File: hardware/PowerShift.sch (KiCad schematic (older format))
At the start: 47 parts

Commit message: RS232 expansion
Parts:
- removed D?: LED_ALT, symbol LED_ALT
- removed J?: I2C, symbol Conn_01x04
- removed R?: 1k, symbol R
- added C1: 100u, symbol C
- added J6: SHIFT_IN, symbol Conn_01x08
- C2, C4: renamed from C?; value C -> 10u
- C3: renamed from C?; value C -> 100u
- J2: renamed from J?; value USB_A -> MICRO_USB
- gave numbers to parts that had none: 40
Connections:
- net labels added: RX, TX, XCK
- wire segments 273 -> 279
- no-connect marks 21 -> 19
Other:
- moved on the sheet: C15, C16, C2, C3, C4, D1, J1, J10, J2, J5, J7, JMP1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

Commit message: JST 5 pin common part
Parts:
- removed J13: Conn_01x04, symbol Conn_01x04
- added J14: JST-ZR, symbol Conn_01x05
- R3: value R -> Rntc
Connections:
- wire segments 279 -> 281
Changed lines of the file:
@@
 P 5300 4750
 F 0 "R3" H 5350 4800 50  0000 L CNN
-F 1 "R" H 5350 4700 50  0000 L CNN
+F 1 "Rntc" H 5350 4700 50  0000 L CNN
 F 2 "" V 5230 4750 50  0001 C CNN
 F 3 "" H 5300 4750 50  0001 C CNN
@@
 	1    0    0    -1
 $EndComp
-$Comp
-L Conn_01x04 J13
-U 1 1 5B31B710
-P 5600 5350
-F 0 "J13" H 5600 5550 50  0000 C CNN
-F 1 "Conn_01x04" H 5600 5050 50  0000 C CNN
-F 2 "" H 5600 5350 50  0001 C CNN
-F 3 "" H 5600 5350 50  0001 C CNN
-	1    5600 5350
-	1    0    0    -1
-$EndComp
-Wire Wire Line
-	4850 5250 5400 5250
-Wire Wire Line
-	4850 5350 5400 5350
-Wire Wire Line
-	4850 5450 5400 5450
+Wire Wire Line
+	4850 5250 5800 5250
+Wire Wire Line
+	4850 5350 5800 5350
+Wire Wire Line
+	4850 5450 5800 5450
 $Comp
 L GND #PWR37
@@
 	5300 4900 5300 5450
 Connection ~ 5300 5450
-Wire Wire Line
-	5400 5550 5300 5550
-Wire Wire Line
-	5300 5550 5300 5650
 $Comp
 L GND #PWR41
 U 1 1 5B31CE60
-P 5300 5650
-F 0 "#PWR41" H 5300 5400 50  0001 C CNN
-F 1 "GND" H 5300 5500 50  0000 C CNN
-F 2 "" H 5300 5650 50  0001 C CNN
-F 3 "" H 5300 5650 50  0001 C CNN
-	1    5300 5650
-	1    0    0    -1
-$EndComp
-Text Label 5200 5550 2    60   ~ 0
+P 5700 5650
+F 0 "#PWR41" H 5700 5400 50  0001 C CNN
+F 1 "GND" H 5700 5500 50  0000 C CNN
+F 2 "" H 5700 5650 50  0001 C CNN
+F 3 "" H 5700 5650 50  0001 C CNN
+	1    5700 5650
+	1    0    0    -1
+$EndComp
+Text Label 5350 5550 2    60   ~ 0
 NTC_EN
 Wire Wire Line
-	5200 5550 4850 5550
+	4850 5550 5350 5550
 Text Label 1800 6150 0    60   ~ 0
 SDA
@@
 Wire Wire Line
 	4050 950  4050 1050
+$Comp
+L Conn_01x05 J14
+U 1 1 5B345A2C
+P 6000 5350
+F 0 "J14" H 6000 5650 50  0000 C CNN
+F 1 "JST-ZR" H 6000 5050 50  0000 C CNN
+F 2 "" H 6000 5350 50  0001 C CNN
+F 3 "" H 6000 5350 50  0001 C CNN
+	1    6000 5350
+	1    0    0    -1
+$EndComp
+$Comp
+L +3.3V #PWR?
+U 1 1 5B345AFF
+P 5700 5050
+F 0 "#PWR?" H 5700 4900 50  0001 C CNN
+F 1 "+3.3V" H 5700 5190 50  0000 C CNN
+F 2 "" H 5700 5050 50  0001 C CNN
+F 3 "" H 5700 5050 50  0001 C CNN
+	1    5700 5050
+	1    0    0    -1
+$EndComp
+Wire Wire Line
+	5800 5150 5700 5150
+Wire Wire Line
+	5700 5150 5700 5050
+Wire Wire Line
+	5800 5550 5700 5550
+Wire Wire Line
+	5700 5550 5700 5650
 $EndSCHEMATC

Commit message: Values
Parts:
- C13, C14, C5, C6, C7, C8: value C -> 100n
- J11, J12, J3, J4, J8, J9: value Conn_01x08 -> JST-ZR
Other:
- moved on the sheet: C13, C14, C5, C6, C7, C8

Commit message: ERC OK
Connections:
- net +3V3: now also U6.1 (OE)
- net VBUS: no longer names the net of J2.1 (VBUS), JMP1.1 (G1)
- no-connect marks 19 -> 21
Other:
- moved on the sheet: JMP1

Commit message: Step down regulator
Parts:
- added C17: 100n, symbol C
- added C18, C20: 22u, symbol C
- added C19: 91p, symbol C
- added L1: 12u, kuro:Bourns_SDR1307_14x14mm, symbol L
- added R5: 100k, symbol R
- added R6: 10.1k, symbol R
- added U10: TPS54302, symbol TPS54302
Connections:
- net GND: now also C18.2, C20.2, R6.2, U10.1 (GND)
- net VPP: now also C19.1, C20.1, L1.1, R5.1; no longer J1.1
- new net: C18.1, J1.1, U10.3 (VIN)
- new net: C17.2, L1.2, U10.2 (SW)
- new net: C19.2, R5.2, R6.1, U10.4 (FB)
- new net: C17.1, U10.6 (BOOT)
- no-connect marks 21 -> 22
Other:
- moved on the sheet: C1, C2, C3, C4, J1, J2, J6, J7, JMP1, R1, R2, U1

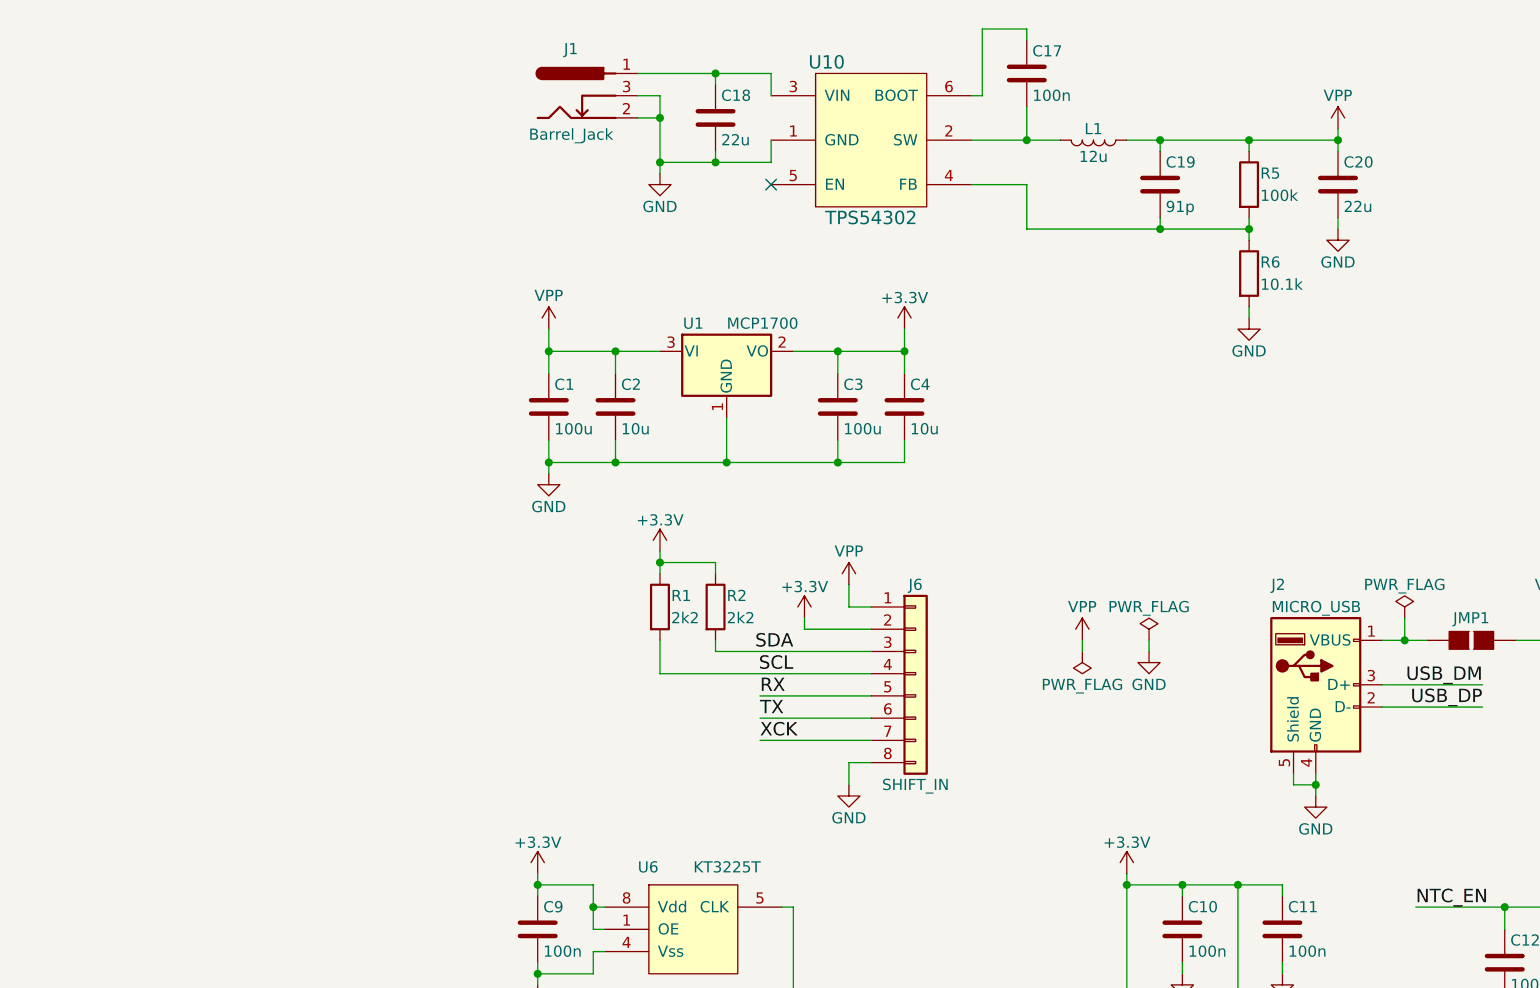
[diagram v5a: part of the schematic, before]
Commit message: Buck reg bypass
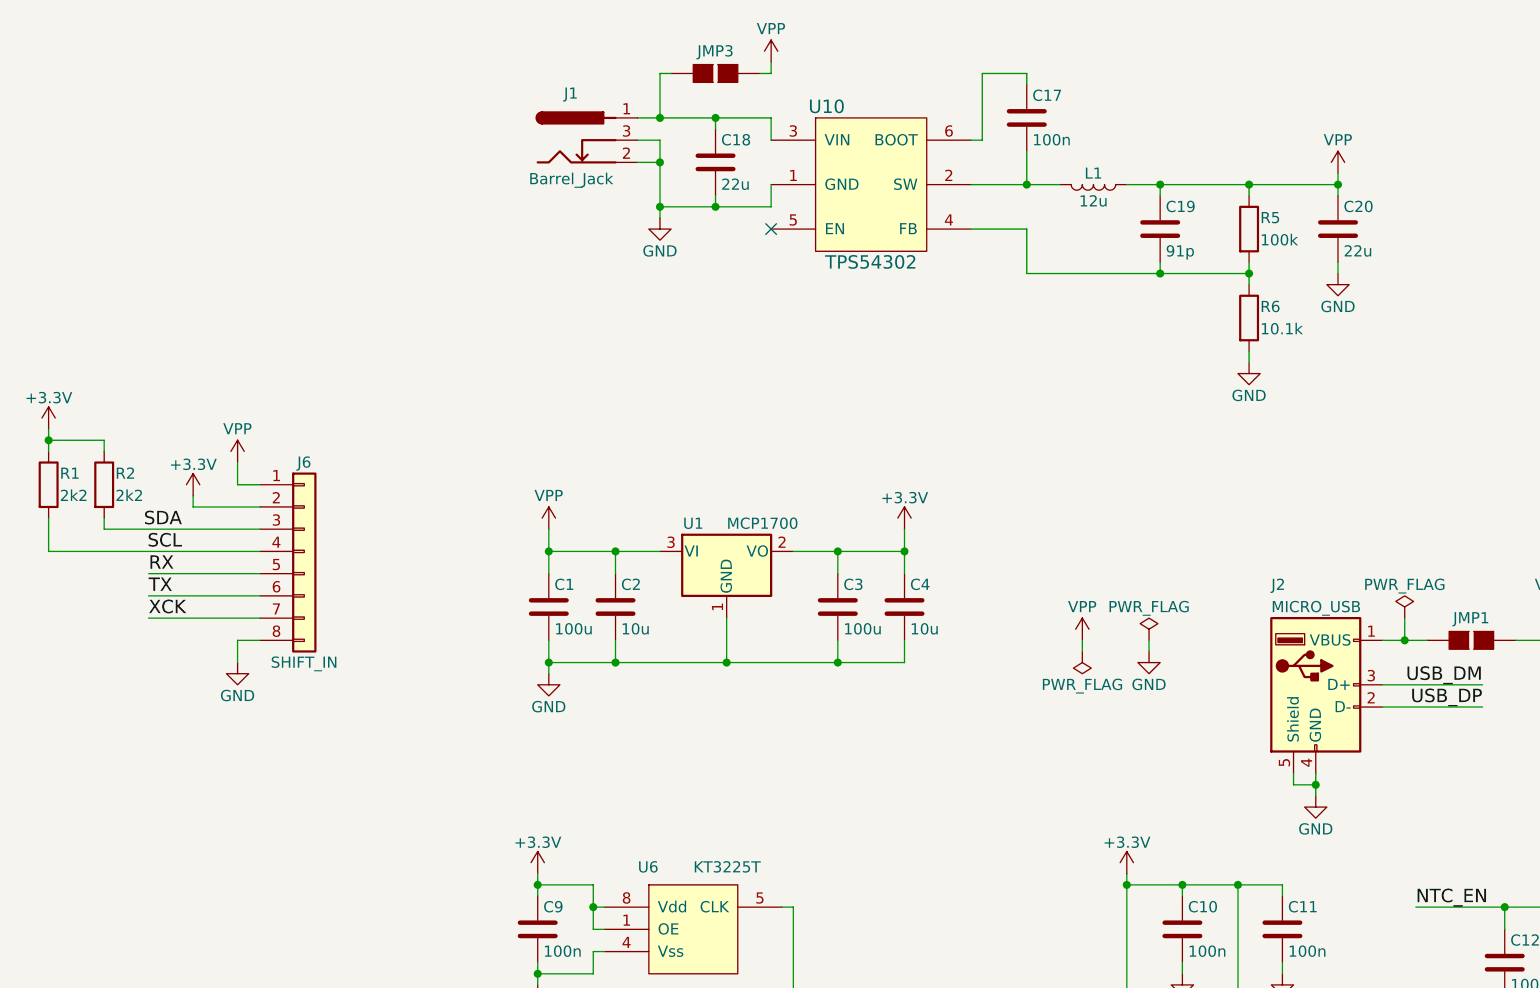
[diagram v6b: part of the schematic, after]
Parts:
- added JMP3: GS2, Connectors:GS2, symbol GS2
- J7: footprint AVR-PDI-6 -> Pin_Headers:Pin_Header_Straight_2x03_Pitch2.54mm
- U9: footprint TQFP32 -> Housings_QFP:TQFP-32_7x7mm_Pitch0.8mm
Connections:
- net VPP: now also JMP3.2 (G2)
- net at C18.1, J1.1, U10.3 (VIN): now also JMP3.1 (G1)
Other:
- moved on the sheet: C1, C17, C18, C19, C2, C20, C3, C4, J1, J6, L1, R1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

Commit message: Footprints
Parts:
- C1, C3: value 100u -> 22u; footprint (none) -> Capacitors_SMD:C_0805_HandSoldering
- C10, C11, C12, C13, C14, C15, C16, C17, C19, C2, C4, C5, C6, C7, C8, C9: footprint (none) -> Capacitors_SMD:C_0603_HandSoldering
- C18, C20: footprint (none) -> Capacitors_SMD:C_0805_HandSoldering
- D1: footprint (none) -> LEDs:LED_0603_HandSoldering
- J10, J11, J12, J3, J4, J5, J6, J8, J9: footprint (none) -> kuro:B8B-ZR-SM4-TF
- J14: footprint (none) -> kuro:B5B-ZR-SM4-TF
- J2: footprint (none) -> kuro:Molex_47346-0001_Micro_USB_SMT
- R1, R2, R3, R4, R5, R6: footprint (none) -> Resistors_SMD:R_0603_HandSoldering
- U10: footprint (none) -> TO_SOT_Packages_SMD:SOT-23-6_Handsoldering
- U2, U3, U4, U5, U7, U8: footprint (none) -> Housings_SOIC:SOIC-20W_7.5x12.8mm_Pitch1.27mm
- U6: footprint (none) -> kuro:KT3225T
- Y1: footprint (none) -> kuro:SMD_Crystal_Multi_QC6CB_7A_ABM7

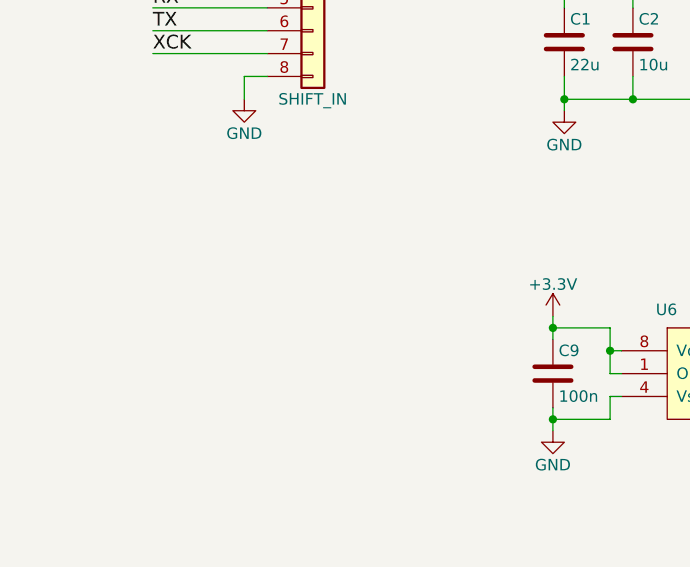
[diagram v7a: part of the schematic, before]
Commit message: Additional shift reg caps
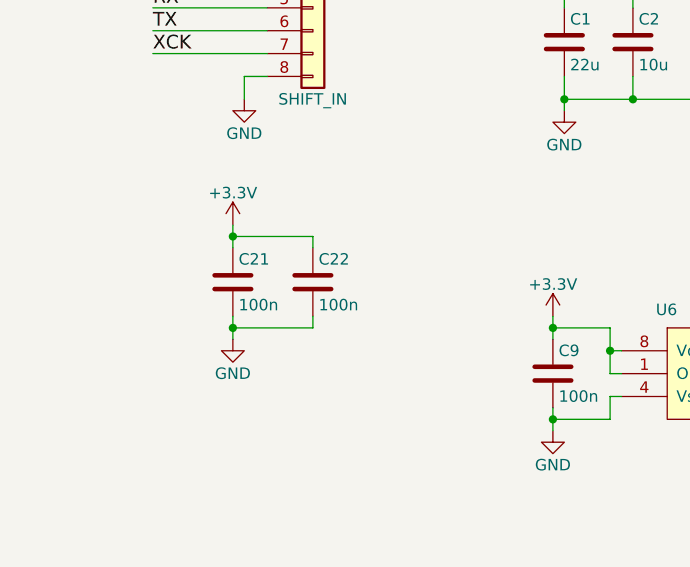
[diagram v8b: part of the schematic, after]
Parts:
- added C21, C22: 100n, Capacitors_SMD:C_0603_HandSoldering, symbol C
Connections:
- net +3V3: now also C21.1, C22.1
- net GND: now also C21.2, C22.2
